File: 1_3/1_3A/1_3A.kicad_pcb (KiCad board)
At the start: 2 copper layers, 137.5 x 93.4 mm, 52 parts, among them SW1 SW_SPST, SW10 SW_SPST, SW11 SW_SPST, SW12 SW_SPST, SW13 SW_SPST, SW14 SW_SPST, SW15 SW_SPST, SW16 SW_SPST, SW17 SW_SPST, SW18 SW_SPST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

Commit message: A chk
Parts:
- moved H4 0.46 mm to (186.2, 116.0)
- moved D21 0.32 mm to (194.6, 125.1)
- moved D2 0.20 mm to (103.5, 86.4)
- moved D7 0.17 mm to (84.5, 90.2)
- moved D8 0.13 mm to (103.5, 90.3)
- moved H1 0.11 mm to (94.0, 85.7)
- moved H2 0.11 mm to (94.0, 104.7)
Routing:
- net R1: track 185.0 -> 186.3 mm
- net Net-(D7-A): track 15.7 -> 16.7 mm

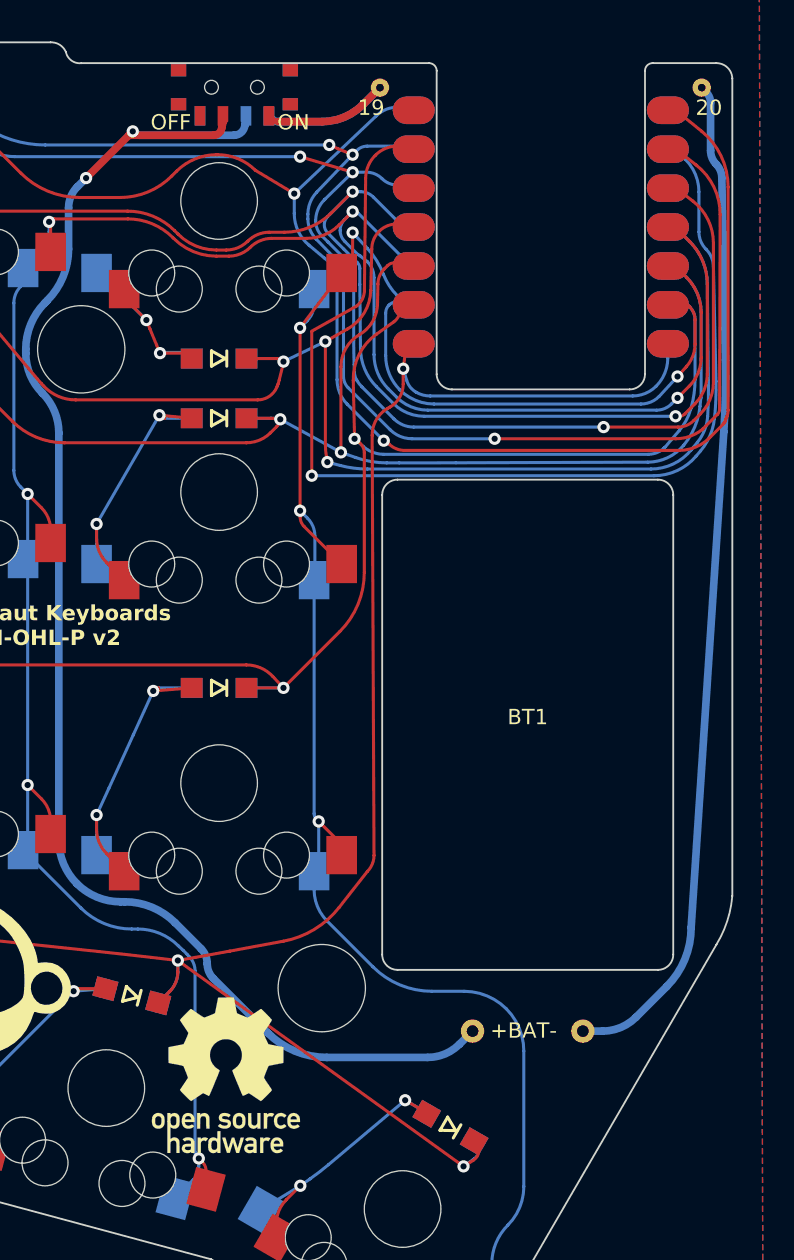
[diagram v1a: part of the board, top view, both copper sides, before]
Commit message: adjust d19,20,21 all
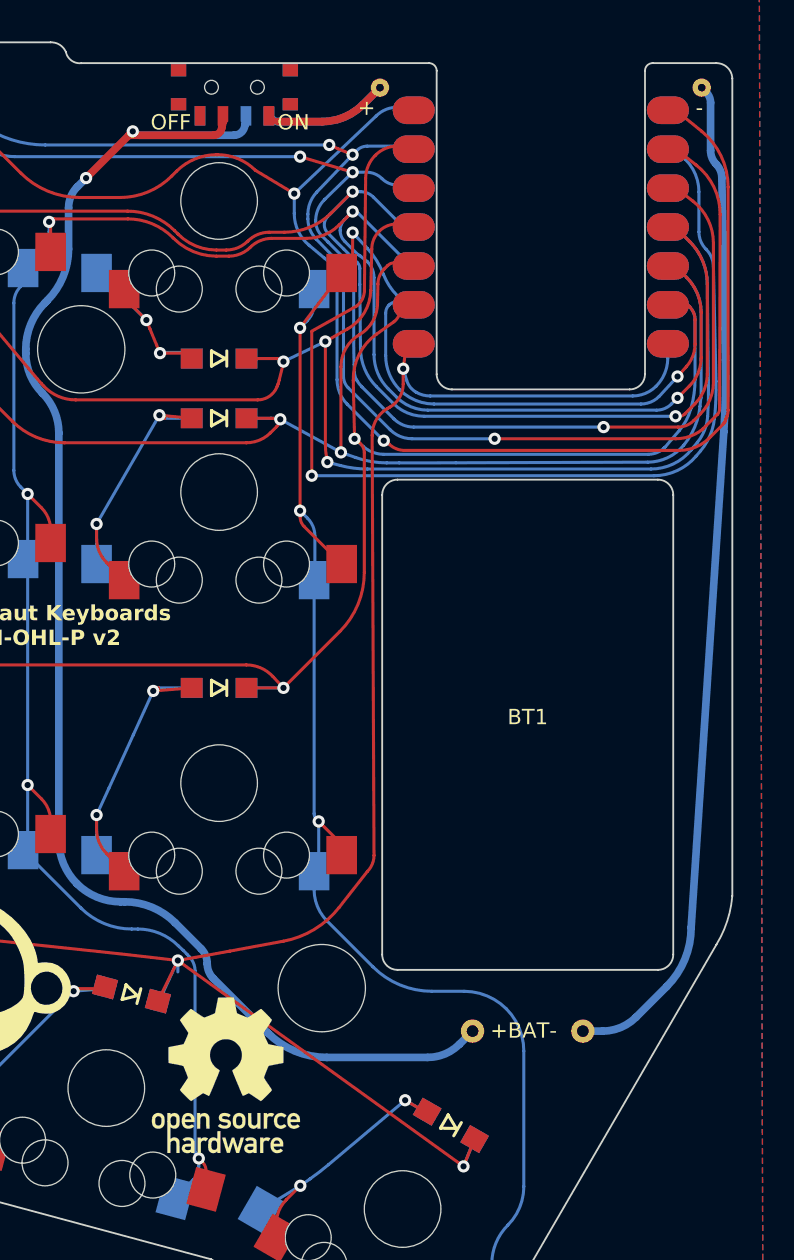
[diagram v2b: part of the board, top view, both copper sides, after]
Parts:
- moved D21 0.15 mm to (194.6, 125.0)
- moved D20 0.11 mm to (173.8, 116.4)
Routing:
- net R3: track 128.7 -> 129.8 mm
